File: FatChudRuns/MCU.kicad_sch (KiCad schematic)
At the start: 20 parts, among them J2 Z-21320110021001, J3 FTSH-107-01-L-DV-K-P, SW1 SW_Push, SW2 SW_DIP_x01, U1 STM32F107RBT6

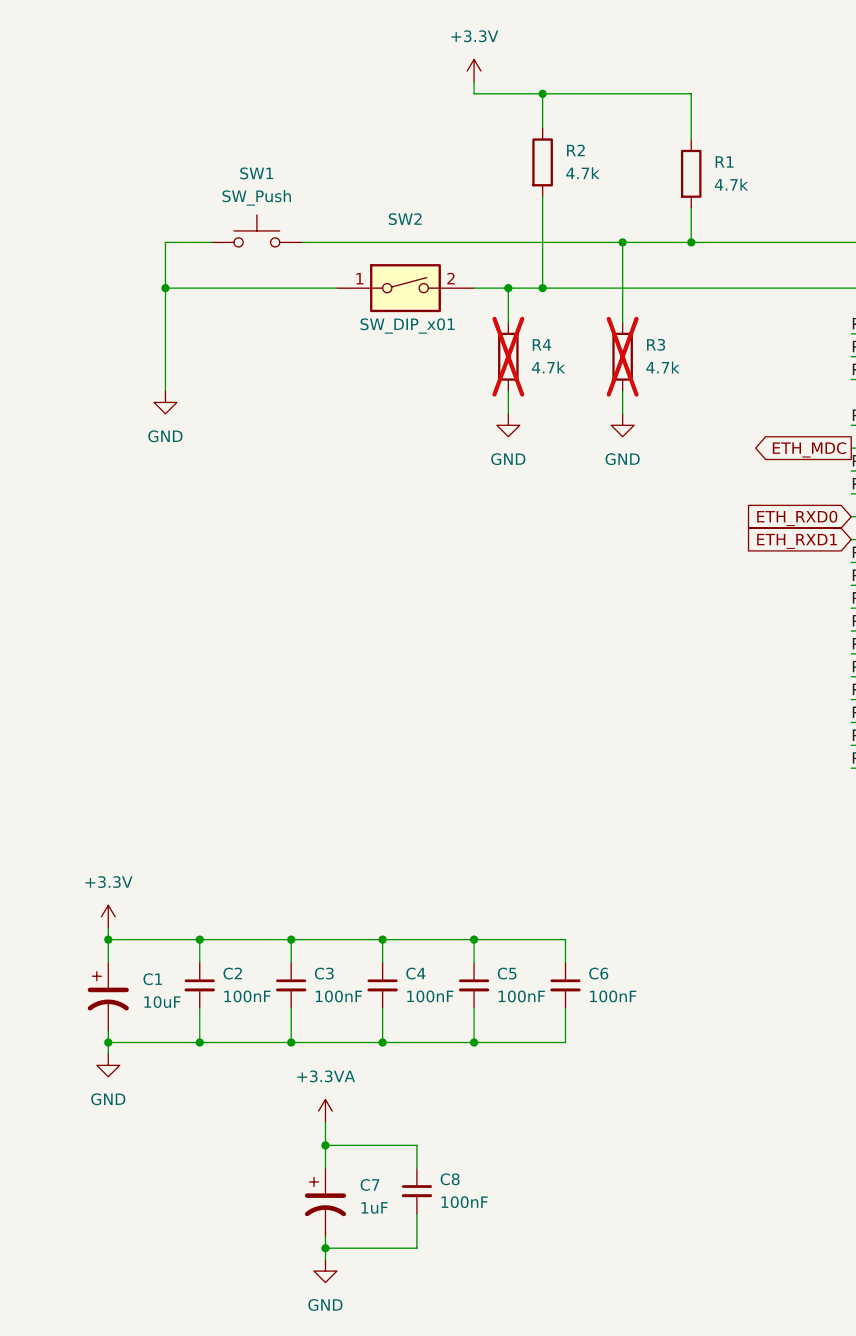
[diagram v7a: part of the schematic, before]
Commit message: added caps and diode footprints, all caps now non-polarized ceramic caps
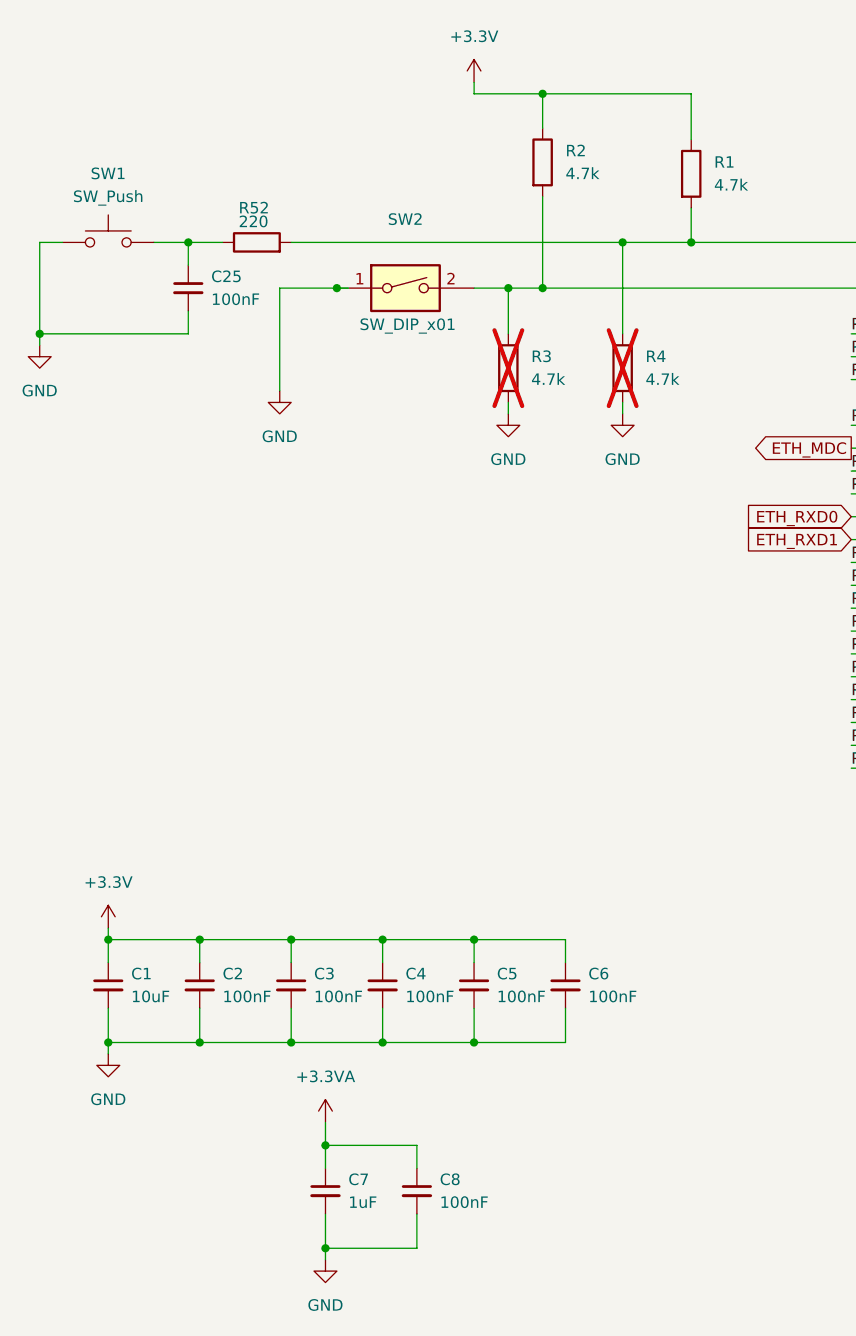
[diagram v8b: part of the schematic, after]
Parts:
- removed C1: 10uF, symbol Device:C_Polarized_US
- removed C7: 1uF, symbol Device:C_Polarized_US
- added C1: 10uF, Capacitor_SMD:C_0603_1608Metric, symbol Device:C_Small
- added C25: 100nF, Capacitor_SMD:C_0603_1608Metric, symbol Device:C_Small
- added C7: 1uF, Capacitor_SMD:C_0603_1608Metric, symbol Device:C_Small
- added R52: 220, Resistor_SMD:R_0603_1608Metric, symbol Device:R
- C2, C3, C4, C5, C6, C8: footprint (none) -> Capacitor_SMD:C_0603_1608Metric
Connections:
- net +3.3V: now also C1.1
- net +3.3VA: now also C7.1
- net GND: now also C1.2, C25.2, C7.2
- net at R1.2, U1.7 (NRST): now also R4.1, R52.2; no longer R3.1, SW1.2
- net at R2.2, SW2.2, U1.60 (BOOT0): now also R3.1; no longer R4.1
- new net: C25.1, R52.1, SW1.2
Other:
- moved on the sheet: SW1
